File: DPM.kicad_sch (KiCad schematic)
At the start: 43 parts, among them J1 Conn_02x12_Odd_Even, J2 Conn_02x05_Odd_Even, U1 74LS251, U2 74LVC2G74, U25 74LS85, U28 74LS85, U3 ADG333A, U31 74LS85, U4 MCP23017_SP, U5 ADG333A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

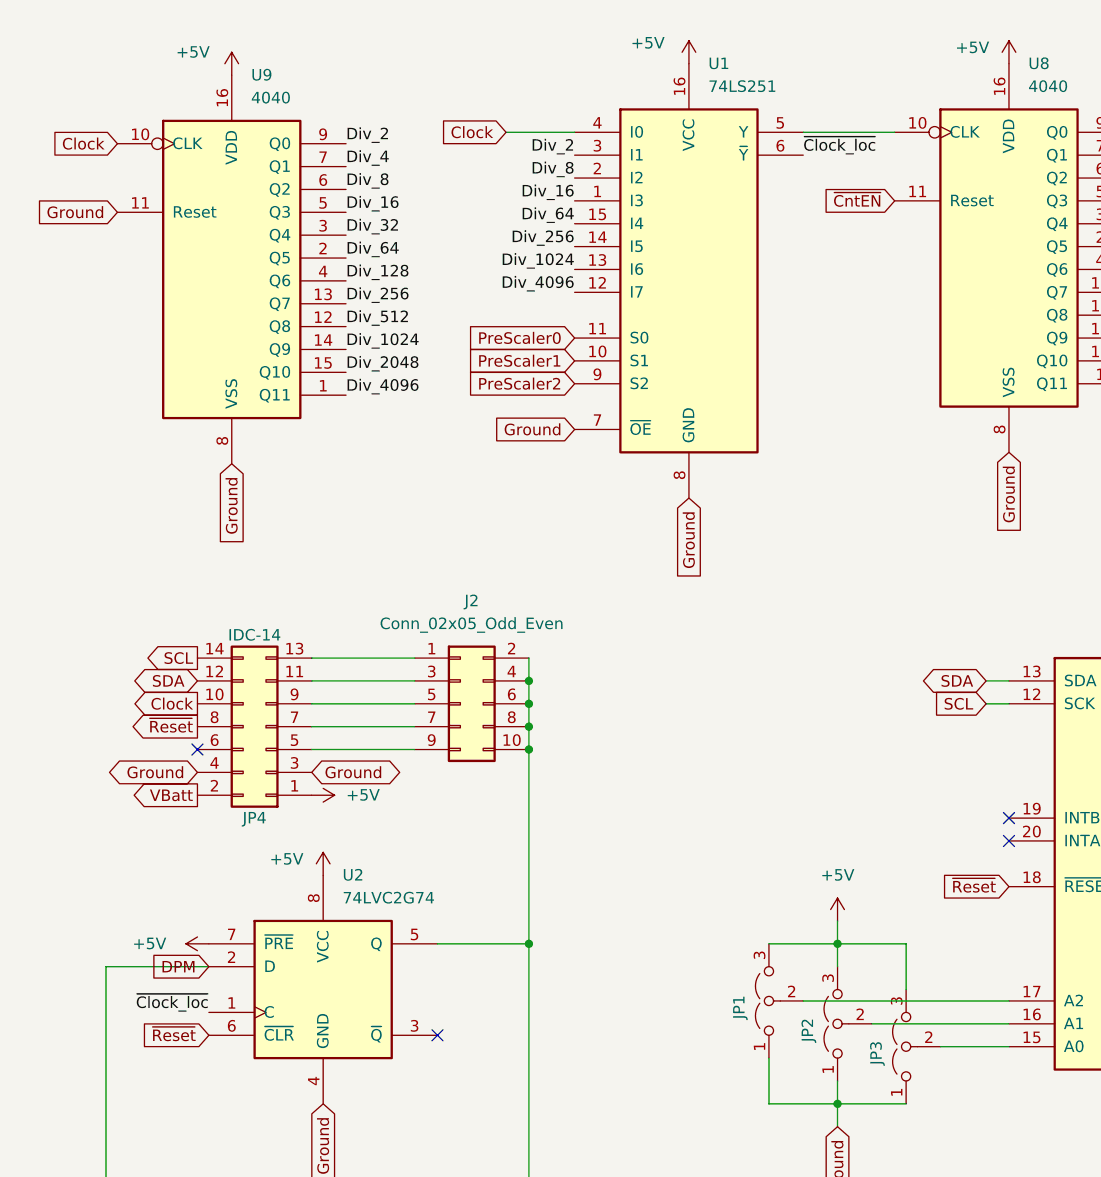
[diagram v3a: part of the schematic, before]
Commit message: Correction clock du 2G74 Reroutage léger
git-svn-id: file:///D%5C00%20-%20Dev%20&%20Calculs%5CRepoTortoiseSVN_PCB%5CD-DPM/trunk@23 f29d8339-a183-0348-962e-9e4594cf8312
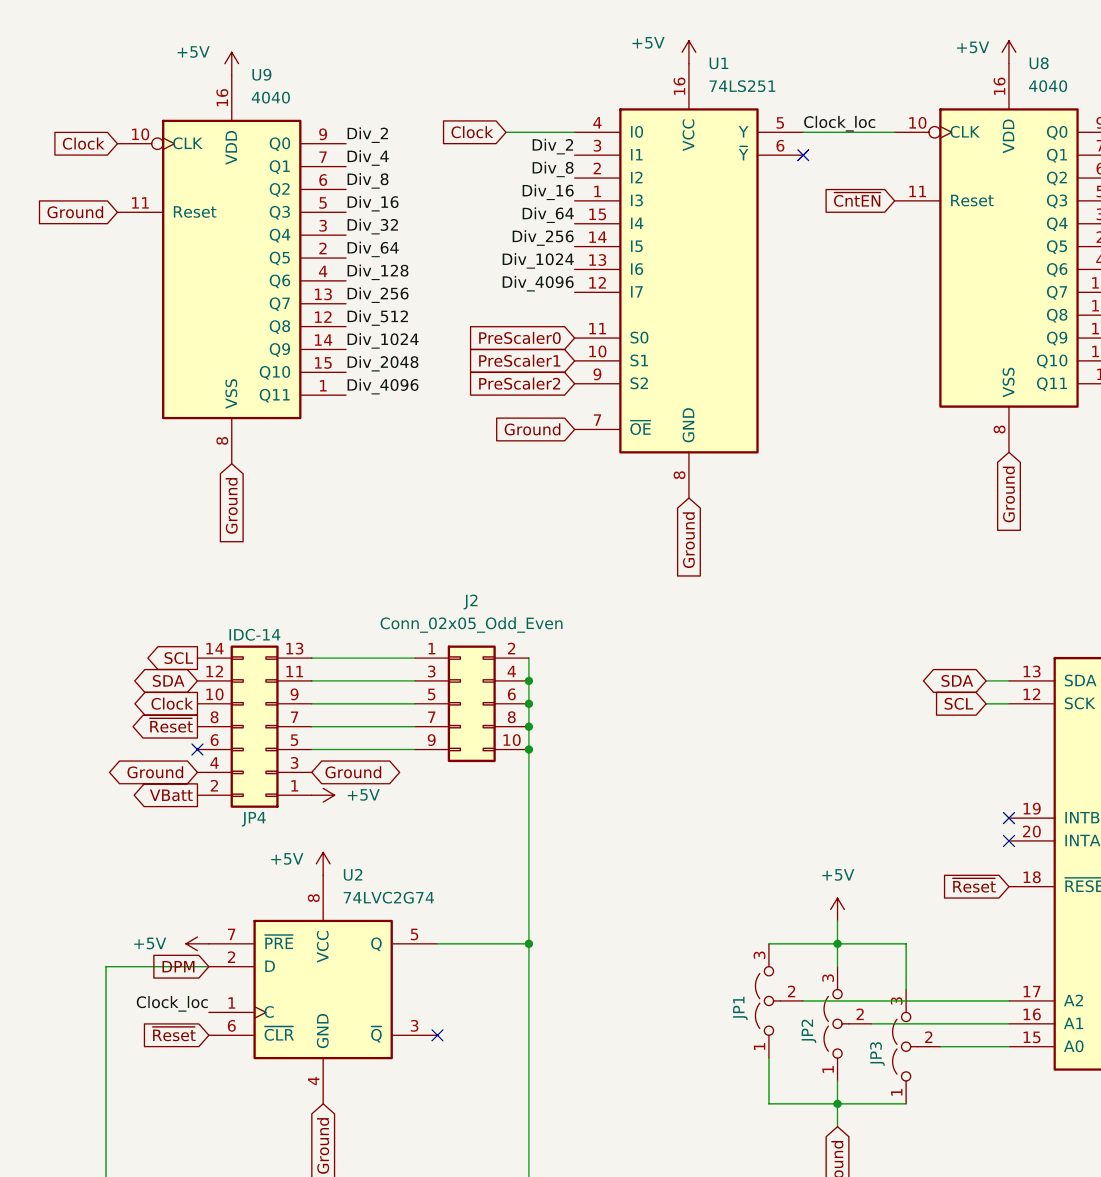
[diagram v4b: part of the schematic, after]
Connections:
- net Clock_loc: now reaches U1.5 (Y), U8.10 (CLK)
- net Clock_loc: now also U2.1 (C)
- net ~{Clock_loc}: no longer names the net of U1.6 (~{Y})
- net ~{Clock_loc}: no longer U2.1 (C)
- no-connect marks 6 -> 7

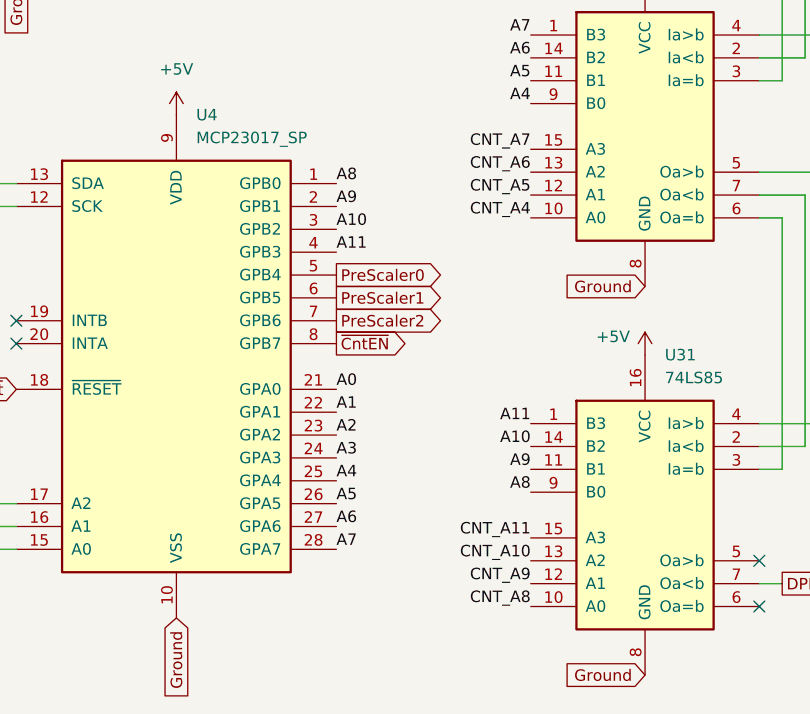
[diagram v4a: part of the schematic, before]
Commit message: Modification : PinOut des ports GPIOA et GPIOB
git-svn-id: file:///D%5C00%20-%20Dev%20&%20Calculs%5CRepoTortoiseSVN_PCB%5CD-DPM/trunk@24 f29d8339-a183-0348-962e-9e4594cf8312
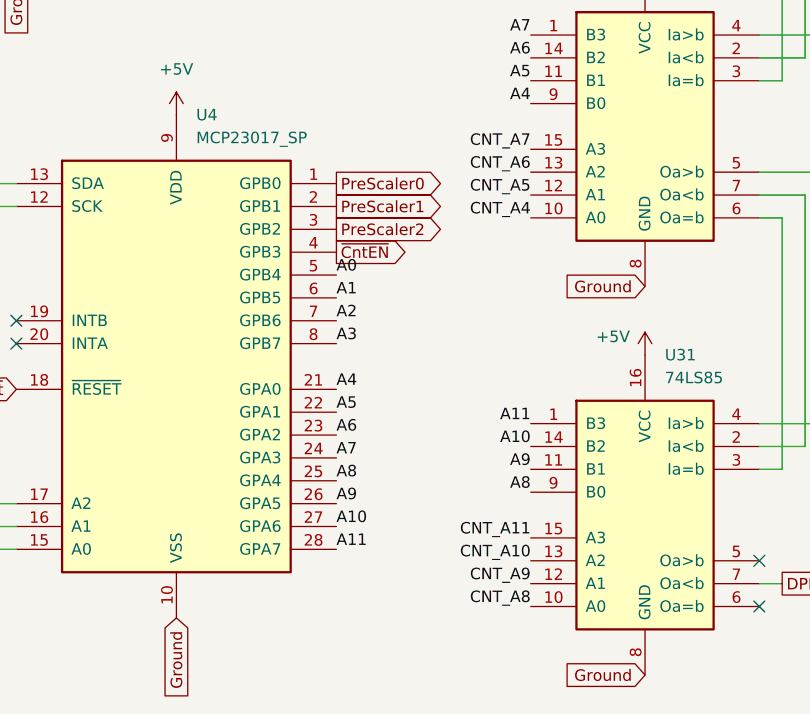
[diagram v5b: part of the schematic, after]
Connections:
- net A0: now also U4.5 (GPB4); no longer U4.21 (GPA0)
- net A1: now also U4.6 (GPB5); no longer U4.22 (GPA1)
- net A10: now also U4.27 (GPA6); no longer U4.3 (GPB2)
- net A11: now also U4.28 (GPA7); no longer U4.4 (GPB3)
- net A2: now also U4.7 (GPB6); no longer U4.23 (GPA2)
- net A3: now also U4.8 (GPB7); no longer U4.24 (GPA3)
- net A4: now also U4.21 (GPA0); no longer U4.25 (GPA4)
- net A5: now also U4.22 (GPA1); no longer U4.26 (GPA5)
- net A6: now also U4.23 (GPA2); no longer U4.27 (GPA6)
- net A7: now also U4.24 (GPA3); no longer U4.28 (GPA7)
- net A8: now also U4.25 (GPA4); no longer U4.1 (GPB0)
- net A9: now also U4.26 (GPA5); no longer U4.2 (GPB1)
- net PreScaler0: now also U4.1 (GPB0); no longer U4.5 (GPB4)
- net PreScaler1: now also U4.2 (GPB1); no longer U4.6 (GPB5)
- net PreScaler2: now also U4.3 (GPB2); no longer U4.7 (GPB6)
- net ~{CntEN}: now also U4.4 (GPB3); no longer U4.8 (GPB7)
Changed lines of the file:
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@@
 			"AGcAQQBBAEQALwAyAHcAQgBEAEEAQQBNAEMAQQBnAE0AQwBBAGcATQBEAEEAdwBNAEUAQQB3AE0A"
 			"RQBCAFEAZwBGAEIAUQBRAEUAQgBRAG8ASABCAHcAWQBJAEQAQQBvAE0ARABBAHMASwBDAHcAcwBO"
-			"AEQAaABJAFEARA=="
+			"AEQAaABJAFEARAAAAAAAAAAAAAAAAAAAAAAAAAAAAAAAAAAAAAAAAAAAAAAAAAAAAAAAAAAAAAAA"
+			"AAAAAAAAAAAAAAAAAAAAAAAAAAAAAAAAAAAAAAAAAAAAAAAAAAAAAAAAAAAAAAAAAAAAAAAAAAAA"
+			"AAAAAAAAAAAAAAAAAAAAAAAAAAAAAAAAAAAAAAAAAAAAAAAAAAAAAAAAAAAAAAAAAAAAAAAAAAAA"
+			"AAAAAAAAAAAAAAAAAAAAAAAAAAAAAAAAAAAAAAAAAAAAAAAAAAAAAAAAAAAAAAAAAAAAAAAAAAAA"
+			"AAAAAAAAAAAAAAAAAAAAAAAAAAAAAAAAAAAAAAAAAAAAAAAAAAAAAAAAAAAAAAAAAAAAAAAAAAAA"
+			"AAAAAAAAAAAAAAAAAAAAAAAAAAAAAAAAAAAAAAAAAAAAAAAAAAAAAAAAAAAAAAAAAAAAAAAAAAAA"
+			"AAAAAAAAAAAAAAAAAAAAAAAAAAAAAAAAAAAAAAAAAAAAAAAAAAAAAAAAAAAAAAAAAAAAAAAAAAAA"
+			"AAAAAAAAAAAAAAAAAAAAAAAAAAAAAAAAAAAAAAAAAAAAAAAAAAAAAAAAAAAAAAAAAAAAAAAAAAAA"
+			"AAAAAAAAAAAAAAAAAAAAAAAAAAAAAAAAAAAAAAAAAAAAAAAAAAAAAAAAAAAAAAAAAAAAAAAAAAAA"
+			"AAAAAAAAAAAAAAAAAAAAAAAAAAAAAAAAAAAAAAAAAAAAAAAAAAAAAAAAAAAAAAAAAAAAAAAAAAAA"
+			"AAAAAAAAAAAAAAAAAAAAAAAAAAAAAAAAAAAAAAAAAAAAAAAAAAAAAAAAAAAAAAAAAAAAAAAAAAAA"
+			"AAAAAAAAAAAAAAAAAAAAAAAAAAAAAAAAAAAAAAAAAAAAAAAAAAAAAAAAAAAAAAAAAAAAAAAAAAAA"
+			"AAAAAAAAAAAAAAAAAAAAAAAAAAAAAAAAAAAAAAAAAAAAAAAAAAAAAAAAAAAAAAAAAAAAAAAAAAAA"
+			"AAAAAAAAAAAAAAAAAAAAAAAAAAAAAAAAAAAAAAAAAAAAAAAAAAAAAAAAAAAAAAAAAAAAAAAAAAAA"
+			"AAAAAAAAAAAAAAAAAAAAAAAAAAAAAAAAAAAAAAAAAAAAAAAAAAAAAAAAAAAAAAAAAAAAAAAAAAAA"
+			"AAAAAAAAAAAAAAAAAAAAAAAAAAAAAAAAAAAAAAAAAAAAAAAAAAAAAAAAAAAAAAAAAAAAAAAAAAAA"
+			"AAAAAAAAAAAAAAAAAAAAAAAAAAAAAAAAAAAAAAAAAAAAAAAAAAAAAAAAAAAAAAAAAAAAAAAAAAAA"
+			"AAAAAAAAAAAAAAAAAAAAAAAAAAAAAAAAAAAAAAAAAAAAAAAAAAAAAAAAAAAAAAAAAAAAAAAAAAAA"
+			"AAAAAAAAAAAAAA=="
 		)
 	)
@@
 			"agByAEUAVgBxAFYAUwBHADcAdABXAFMAUwAyAG4ARQBSAGMAawBoAEoASQBvADIASwA3AHYAbQBB"
 			"AEkAeQBNADEAawA2AFgAKwB6AHgATABvAEcAbABhAGIAWQBXAG0AdABmAGIAbwA3AEQAeABIAGIA"
-			"NgB0AGIAeQAzADgAZQBaAA=="
+			"NgB0AGIAeQAzADgAZQBaAABqAICQrP9KqgIAAJCs/0qqAgAAkKz/SqoCAACQrP9KqgIAAJCs/0qq"
+			"AgAAkKz/SqoCAACQrP9KqgIAAJCs/0qqAgAAkKz/SqoCAACQrP9KqgIAAJCs/0qqAgAAkKz/SqoC"
+			"AACQrP9KqgIAAJCs/0qqAgAAkKz/SqoCAACQrP9KqgIAAAAAAAAAAAAA4hHk/QBrAICggf1KqgIA"
+			"AKCB/UqqAgAAoIH9SqoCAACggf1KqgIAAKCB/UqqAgAAoIH9SqoCAACggf1KqgIAAKCB/UqqAgAA"
+			"oIH9SqoCAACggf1KqgIAAKCB/UqqAgAAoIH9SqoCAACggf1KqgIAAKCB/UqqAgAAoIH9SqoCAACg"
+			"gf1KqgIAAAAAAAAAAAAA/RH9/QBsAIAAAAAAAAAAAFDF/0qqAgAAAAAAAAAAAAAAAAAAAAAAAAAA"
+			"AAAAAAAAAAAAAAAAAAAAAAAAAAAAAAAAAAAAAAAAAAAAAAAAAAAAAAAAAAAAAAAAAAAAAAAAAAAA"
+			"AAAAAAAAAAAAAAAAAAAAAAAAAAAAAAAAAAAAAAAAAAAAAAAAAAAAAAAAAAAA9BH2/QBtAIBwvf9K"
+			"qgIAAHC9/0qqAgAAcL3/SqoCAABwvf9KqgIAAHC9/0qqAgAAcL3/SqoCAABwvf9KqgIAAHC9/0qq"
+			"AgAAcL3/SqoCAABwvf9KqgIAAHC9/0qqAgAAcL3/SqoCAABwvf9KqgIAAHC9/0qqAgAAcL3/SqoC"
+			"AABwvf9KqgIAAAAAAAAAAAAAzxHP/QBuAICwv/9KqgIAALC//0qqAgAAsL//SqoCAACwv/9KqgIA"
+			"ALC//0qqAgAAsL//SqoCAACwv/9KqgIAALC//0qqAgAAsL//SqoCAACwv/9KqgIAALC//0qqAgAA"
+			"sL//SqoCAACwv/9KqgIAALC//0qqAgAAsL//SqoCAACwv/9KqgIAAAAAAAAAAAAAxhHA/QBvAIBg"
+			"gf1KqgIAAGCB/UqqAgAAYIH9SqoCAABggf1KqgIAAGCB/UqqAgAAYIH9SqoCAABggf1KqgIAAGCB"
+			"/UqqAgAAYIH9SqoCAABggf1KqgIAAGCB/UqqAgAAYIH9SqoCAABggf1KqgIAAGCB/UqqAgAAYIH9"
+			"SqoCAABggf1KqgIAAAAAAAAAAAAA0RHZ/QBwAICQx/9KqgIAAJDH/0qqAgAAkMf/SqoCAAABAQAA"
+			"AAAAAAAAAAAAAAAAAAAAAAAAAAAAAAAAAAAAAAAAAAAAAAAAAAAAAAAAAAAAAAAAAAAAAAAAAAAA"
+			"AAAAAAAAAAAAAAAAAAAAAAAAAAAAAAAAAAAAAAAAAAAAAAAAAAAAAAAAAAAAAAAAAAAAAAAAAAAA"
+			"AAAAAAAAAAAAAAAAAAAAAA=="
 		)
 	)
@@
 			"AHcARAA0AGQAMQAvAHcAegBwAE4AcgBvAFAAawBhAFIANABhAG4AOABpADYAbQBzAE4AUABzADQA"
 			"WQA0AHIAKwAxADIAZgB1AG8AWABWAGsAeQBrAGUAQQBuAEMANwBUAHQAWABiAHcATwBLADcAaQBj"
-			"AFoAZwBrAEcAMQAzAHkAcAArAFcATgB0AHIASABqAG8ARABrAFkAUAB2AGsAVgA0AA=="
+			"AFoAZwBrAEcAMQAzAHkAcAArAFcATgB0AHIASABqAG8ARABrAFkAUAB2AGsAVgA0AAAAAAAAAAAA"
+			"AAAAAAAAAAAAAAAAAAAAAAAAAAAAAAAAAAAAAAAAAAAAAAAAAAAAAAAAAAAAAAAAAAAAAAAAAAAA"
+			"AAAAAAAAAAAAAAAAAAAAAAAAAAAAAAAAAAAAAAAAAAAAAAAAAAAAAAAAAAAAAAAAAAAAAAAAAAAA"
+			"AAAAAAAAAAAAAAAAAAAAAAAAAAAAAAAAAAAAAAAAAAAAAAAAAAAAAAAAAAAAAAAAAAAAAAAAAAAA"
+			"AAAAAAAAAAAAAAAAAAAAAAAAAAAAAAAAAAAAAAAAAAAAAAAAAAAAAAAAAAAAAAAAAAAAAAAAAAAA"
+			"AAAAAAAAAAAAAAAAAAAAAAAAAAAAAAAAAAAAAAAAAAAAAAAAAAAAAAAAAAAAAAAAAAAAAAAAAAAA"
+			"AAAAAAAAAAAAAAAAAAAAAAAAAAAAAAAAAAAAAAAAAAAAAAAAAAAAAAAAAAAAAAAAAAAAAAAAAAAA"
+			"AAAAAAAAAAAAAAAAAAAAAAAAAAAAAAAAAAAAAAAAAAAAAAAAAAAAAAAAAAAAAAAAAAAAAAAAAAAA"
+			"AAAAAAAAAAAAAAAAAAAAAAAAAAAAAAAAAAAAAAAAAAAAAAAAAAAAAAAAAAAAAAAAAAAAAAAAAAAA"
+			"AAAAAAAAAAAAAAAAAAAAAAAAAAAAAAAAAAAAAAAAAAAAAAAAAAAAAAAAAAAAAAAAAAAAAAAAAAAA"
+			"AAAAAAAAAAAAAAAAAAAAAAAAAAAAAAAAAAAAAAAAAAAAAAAAAAAAAAAAAAAAAAAAAAAAAAAAAAAA"
+			"AAAAAAAAAAAAAAAAAAAAAAAAAAAAAAAAAAAAAAAAAAAAAAAAAAAAAAAAAAAAAAAAAAAAAAAAAAAA"
+			"AAAAAAAAAAAAAAAAAAAAAAAAAAAAAAAAAAAAAAAAAAAAAAAAAAAAAAAAAAAAAAAAAAAAAAAAAAAA"
+			"AAAAAAAAAAAAAAAAAAAAAAAAAAAAAAAAAAAAAAAAAAAAAAAAAAAAAAAAAAAAAAAAAAAAAAAAAAAA"
+			"AAAAAAAAAAAAAAAAAAAAAAAAAAAAAAAAAAAAAAAAAAAAAAAAAAAAAAAAAAAAAAAAAAAAAAAAAAAA"
+			"AAAAAAAAAAAAAAAAAAAAAAAAAAAAAAAAAAAAAAAAAAAAAAAAAAAAAAAAAAAAAAAAAAAAAAAAAAAA"
+			"AAAAAAAAAAAAAAAAAAAAAAAAAAAAAAAAAAAAAAAAAAAAAAAAAAAAAAAAAAAAAAAAAAAAAAAAAAAA"
+			"AAAAAAAAAAAAAAAAAAAAAAAAAAAAAAAAAAAAAAAAAAAAAAAAAAAAAAAAAAAAAAAAAAAAAAAAAAAA"
+			"AAAAAAAAAAAAAAAAAAAAAAAAAAAAAAAAAAAAAAAAAAAAAAAAAAAAAAAAAAAAAAAAAA=="
 		)
 	)
@@
 			"dgBaADAAdABiAE8AMQBpAGUAZQBlAGUAUQA0AFcATwBOAFEAVwBaAGkAZQB3AEEAQgBOAGMAWgBw"
 			"AFgAeABBACsASABYAGoAMwBTAHQATwBoAGkAMQBiAFEATgBRAGgAOABSADIAUwBhAHIAQgBwADEA"
-			"egBOAEMAWgBMAHkAQQ=="
+			"egBOAEMAWgBMAHkAQQByAHUARQBwAGgAWQA1AFkAQQBKAHkAUwBEAGoAWQBjAC8AZAA0ADcAVABV"
+			"AEwAUQBYADkAaABjADIAeABZAG8ASgBvAG0AagBMAEEAWgB4AGsARQBaAC8AVwB2AG4AcgBRAGYA"
+			"MgBZAGQAZgAwADcAUgBiAEwAUgByAHIAeABGAHAAYwB0AGcAYgBqAFMANwArADgAbgBpADAAKwBR"
+			"AFgAUAAyAGkAeABzADQAYgBXAE4ASQBYAE0AaABDAFIATwBMAGEASgBtAEIAQgBJADMAegBxAE0A"
+			"aQBUAEsAZwBIAHIAOQA3ADQAdAA4AEMAYQAxADQAUgBrADEAUwA3ADEAbgB3ADcAZgArAEYANAAz"
+			"AGEARgA3ADIAYQA2AGcAawBzAGwAZABjAG8AeQBGAHkAUwBnAEkANQBVAGoAUABIAEkAcQBDADMA"
+			"OABhAC8ARAByAFUANwBPADYAdQA0AE4AZQA4AEwAMwBkAHIAcABjAFYAdgBlAFQAegB4ADMAbABz"
+			"ADYAVwBrAGUAQwBiAGUAVgAyAEIAeABHAHUAQwBTAGoASABBAHcAZQBEAFcAUwBQAGcANgBpAC8A"
+			"RABUAHcARAA0AFMAVwA1AHQAMQBUAHcAeABQAHAATQB4AGsARgB2ADgAawAzADIASQB4AG4ANQBW"
+			"AHoAOAB1ADQAeABqAEgAWABIAEgAWABGAGMAUABlAGYAcwB5AGEAbABiADYATgBhADIAMgBqADYA"
+			"LwBhAFcATgB4AGIAeABTAEoAawBXAGgAVQBTAGIAdABYAFQAVQBDAEEAeQB0AHUAagBPAEYAWgBC"
+			"AEkAbgB6AG8AegBiADEASQBJAEYAQQBIAHIARQBHAHUAZQBCAC8ARQBuAGwANgA3AEQAcQBIAGgA"
+			"LwBWAFAASwB0AGsAbABUAFUAawBtAGcAbQAyAFEAUABJAHkAbwB3AGsAQgBPAEUAYQBTAE4AdwBE"
+			"AG4AQgBaAEcAQQA1AEIAcgBoAGQAVgAwAHYANABhAEQANAA2AFcAMQBsAHEAMgBwAGYAWgB2AEYA"
+			"RgByAGEAMgBsADkAWQBhAFYAZgAzADQAagB0AFoAZgBPAFcANQB0AFkAaABiAHcAcwAzAHoATQBG"
+			"AHQANQBnAFkAbABHAHcARgBsAGYAYgB2AGIAZABYAEUAYQBEACsAegBsAHEAKwBnACsATABQAEEA"
+			"KwBtAHkAWABNADEALwBwADkAcABmAGEAbABxADIAdQA2AGcAZwBiADcAUABkAHgAUwBhAGgALwBh"
+			"AEYAcABiAEYAcABaAHAASgBuAGwAaQB1AHgARwB3AFoAaQB3AFoAUABPADMATQBDADQARgBkADMA"
+			"OABSAFAAZwBqAHEAZg=="
 		)
 	)
@@
 	)
 	(label "A4"
-		(at 157.48 120.65 0)
+		(at 157.48 110.49 0)
 		(effects
 			(font
@@
 	)
 	(label "A5"
-		(at 157.48 123.19 0)
+		(at 157.48 113.03 0)
 		(effects
 			(font
@@
 	)
 	(label "A9"
-		(at 157.48 90.17 0)
+		(at 157.48 123.19 0)
 		(effects
 			(font
@@
 	)
 	(label "A7"
-		(at 157.48 128.27 0)
+		(at 157.48 118.11 0)
 		(effects
 			(font
@@
 	)
 	(label "A8"
-		(at 157.48 87.63 0)
+		(at 157.48 120.65 0)
 		(effects
 			(font
@@
 	)
 	(label "A3"
-		(at 157.48 118.11 0)
+		(at 157.48 105.41 0)
 		(effects
 			(font
@@
 	)
 	(label "A11"
-		(at 157.48 95.25 0)
+		(at 157.48 128.27 0)
 		(effects
 			(font
@@
 	)
 	(label "A0"
-		(at 157.48 110.49 0)
+		(at 157.48 97.79 0)
 		(effects
 			(font
@@
 	)
 	(label "A2"
-		(at 157.48 115.57 0)
+		(at 157.48 102.87 0)
 		(effects
 			(font
@@
 	)
 	(label "A10"
-		(at 157.48 92.71 0)
+		(at 157.48 125.73 0)
 		(effects
 			(font
@@
 	)
 	(label "A6"
-		(at 157.48 125.73 0)
+		(at 157.48 115.57 0)
 		(effects
 			(font
@@
 	)
 	(label "A1"
-		(at 157.48 113.03 0)
+		(at 157.48 100.33 0)
 		(effects
 			(font
@@
 	(global_label "PreScaler1"
 		(shape output)
-		(at 157.48 100.33 0)
+		(at 157.48 90.17 0)
 		(fields_autoplaced yes)
 		(effects
@@
 		)
 		(property "Intersheetrefs" "${INTERSHEET_REFS}"
-			(at 170.8066 100.33 0)
+			(at 170.8066 90.17 0)
 			(effects
 				(font
@@
 	(global_label "~{CntEN}"
 		(shape output)
-		(at 157.48 105.41 0)
+		(at 157.48 95.25 0)
 		(fields_autoplaced yes)
 		(effects
@@
 		)
 		(property "Intersheetrefs" "${INTERSHEET_REFS}"
-			(at 166.0894 105.41 0)
+			(at 166.0894 95.25 0)
 			(effects
 				(font
@@
 	(global_label "PreScaler0"
 		(shape output)
-		(at 157.48 97.79 0)
+		(at 157.48 87.63 0)
 		(fields_autoplaced yes)
 		(effects
@@
 		)
 		(property "Intersheetrefs" "${INTERSHEET_REFS}"
-			(at 170.8066 97.79 0)
+			(at 170.8066 87.63 0)
 			(effects
 				(font
@@
 	(global_label "PreScaler2"
 		(shape output)
-		(at 157.48 102.87 0)
+		(at 157.48 92.71 0)
 		(fields_autoplaced yes)
 		(effects
@@
 		)
 		(property "Intersheetrefs" "${INTERSHEET_REFS}"
-			(at 170.8066 102.87 0)
+			(at 170.8066 92.71 0)
 			(effects
 				(font
